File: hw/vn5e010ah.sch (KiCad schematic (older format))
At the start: 5 parts, among them U1001 VN5E010AH

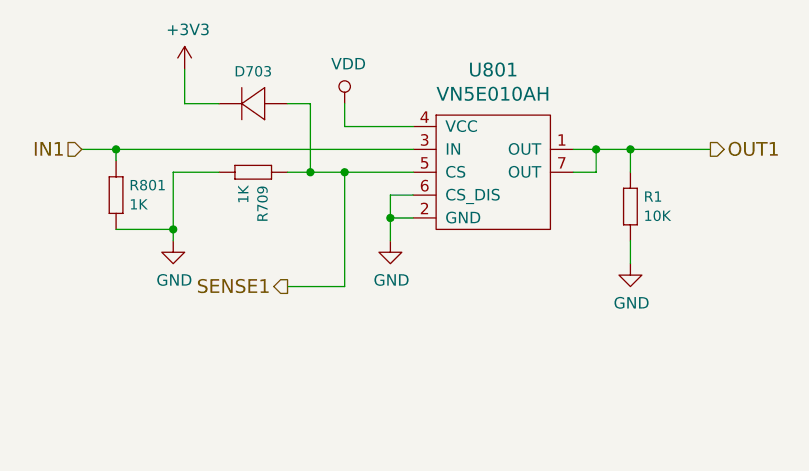
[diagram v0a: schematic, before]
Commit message: sense protection diodes replaced to zeners
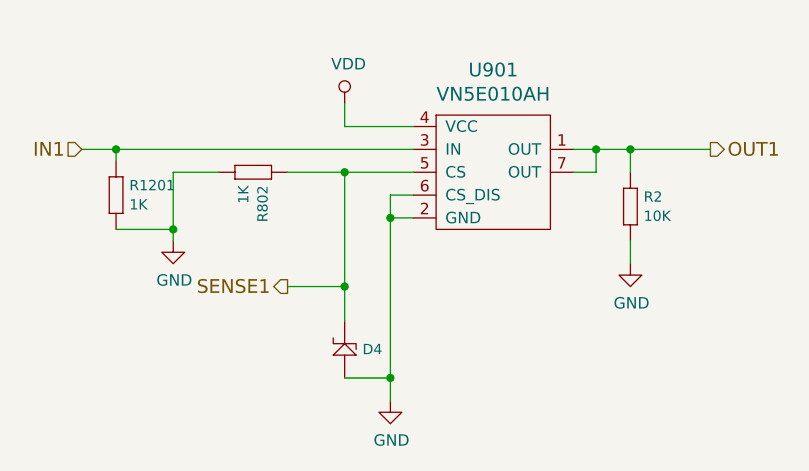
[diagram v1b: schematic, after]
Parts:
- removed D1201: DIODE_RS07J-GS18, usevolt:DO219AB, symbol usevolt:DIODE_RS07J-GS18
- added D3: ZENER_MM3Z3V6T1G, usevolt:SOD-323, symbol usevolt:ZENER_MM3Z3V6T1G
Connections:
- net GND: now also D3.2
- net SENSE1: now also D3.1
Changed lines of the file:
@@
 $Descr A4 11693 8268
 encoding utf-8
-Sheet 7 12
+Sheet 8 12
 Title ""
 Date ""
@@
 SENSE1
 Wire Wire Line
-	4350 3300 4450 3300
-Wire Wire Line
 	3850 3300 4050 3300
 Wire Wire Line
@@
 AR Path="/5A13680F/59D7E637" Ref="#PWR048"  Part="1"
 AR Path="/5A14370A/59D7E637" Ref="#PWR051"  Part="1"
-F 0 "#PWR036" H 4600 2850 50  0001 C CNN
+F 0 "#PWR039" H 4600 2850 50  0001 C CNN
 F 1 "VDD" H 4617 3173 50  0000 C CNN
 F 2 "" H 4600 3000 50  0000 C CNN
@@
 AR Path="/5A13680F/5A014ACD" Ref="#PWR049"  Part="1"
 AR Path="/5A14370A/5A014ACD" Ref="#PWR052"  Part="1"
-F 0 "#PWR037" H 3850 3350 50  0001 C CNN
+F 0 "#PWR040" H 3850 3350 50  0001 C CNN
 F 1 "GND" H 3855 3427 50  0000 C CNN
 F 2 "" H 3850 3600 50  0000 C CNN
@@
 AR Path="/5A13680F/5A058D94" Ref="R1502"  Part="1"
 AR Path="/5A14370A/5A058D94" Ref="R1602"  Part="1"
-F 0 "R801" V 3608 3408 45  0000 L CNN
+F 0 "R1201" V 3608 3408 45  0000 L CNN
 F 1 "1K" V 3692 3408 45  0000 L CNN
 F 2 "yageo:0603" H 3630 3500 20  0001 C CNN
@@
 AR Path="/5A1358B0/5A32CF4A" Ref="U1101"  Part="1"
 AR Path="/5A13680F/5A32CF4A" Ref="U1201"  Part="1"
-F 0 "U801" H 5250 3747 60  0000 C CNN
+F 0 "U901" H 5250 3747 60  0000 C CNN
 F 1 "VN5E010AH" H 5250 3641 60  0000 C CNN
 F 2 "usevolt:HPAK" H 4950 4250 60  0001 C CNN
@@
 L power:GND #PWR044
 U 1 1 5A32CF90
-P 4800 3600
+P 4800 4300
 AR Path="/5A1349CF/5A32CF90" Ref="#PWR044"  Part="1"
 AR Path="/5A14370A/5A32CF90" Ref="#PWR053"  Part="1"
@@
 AR Path="/5A1358B0/5A32CF90" Ref="#PWR047"  Part="1"
 AR Path="/5A13680F/5A32CF90" Ref="#PWR050"  Part="1"
-F 0 "#PWR038" H 4800 3350 50  0001 C CNN
-F 1 "GND" H 4805 3427 50  0000 C CNN
-F 2 "" H 4800 3600 50  0000 C CNN
-F 3 "" H 4800 3600 50  0000 C CNN
-	1    4800 3600
+F 0 "#PWR041" H 4800 4050 50  0001 C CNN
+F 1 "GND" H 4805 4127 50  0000 C CNN
+F 2 "" H 4800 4300 50  0000 C CNN
+F 3 "" H 4800 4300 50  0000 C CNN
+	1    4800 4300
 	1    0    0    -1
 $EndComp
@@
 	3850 3550 3850 3600
 Wire Wire Line
-	4800 3500 4800 3600
+	4800 3500 4800 4200
 $Comp
 L yageo:1K R?
@@
 AR Path="/5A13680F/5B23824A" Ref="R1101"  Part="1"
 AR Path="/5A14370A/5B23824A" Ref="R1202"  Part="1"
-F 0 "R709" V 4258 3358 45  0000 L CNN
+F 0 "R802" V 4258 3358 45  0000 L CNN
 F 1 "1K" V 4342 3358 45  0000 L CNN
 F 2 "yageo:0603" H 4280 3450 20  0001 C CNN
@@
 $EndComp
 $Comp
-L usevolt:DIODE_RS07J-GS18 D1201
-U 1 1 5B23844A
-P 4150 3000
-AR Path="/5A14370A/5B23844A" Ref="D1201"  Part="1"
-AR Path="/5A12FF64/5B23844A" Ref="D703"  Part="1"
-AR Path="/5A130D3E/5B23844A" Ref="D801"  Part="1"
-AR Path="/5A1349CF/5B23844A" Ref="D901"  Part="1"
-AR Path="/5A1358B0/5B23844A" Ref="D1001"  Part="1"
-AR Path="/5A13680F/5B23844A" Ref="D1101"  Part="1"
-F 0 "D703" H 4100 2860 45  0000 C CNN
-F 1 "DIODE_RS07J-GS18" H 4170 2940 45  0001 L BNN
-F 2 "usevolt:DO219AB" H 4180 3150 20  0001 C CNN
-F 3 "http://www.vishay.com/docs/85742/rs07b.pdf" H 4170 3020 60  0001 C CNN
-F 4 "1864882" H 4770 3620 60  0001 C CNN "2nd Source Part Number"
-F 5 "Digi-Key" H 4470 3320 60  0001 C CNN "1st Source"
-F 6 "Farnell" H 4670 3520 60  0001 C CNN "2nd Source"
-F 7 "RS07J-GS18" H 4370 3220 60  0001 C CNN "Manufacturer Part Number"
-F 8 "RS07J-GS18-ND" H 4570 3420 60  0001 C CNN "1st Source Part Number"
-F 9 "Vishay Semiconductor Diodes Division" H 4270 3120 60  0001 C CNN "Manufacturer"
-	1    4150 3000
-	-1   0    0    1
-$EndComp
-$Comp
-L power:+3V3 #PWR0107
-U 1 1 5B23856B
-P 3900 2850
-AR Path="/5A14370A/5B23856B" Ref="#PWR0107"  Part="1"
-AR Path="/5A12FF64/5B23856B" Ref="#PWR0102"  Part="1"
-AR Path="/5A130D3E/5B23856B" Ref="#PWR0103"  Part="1"
-AR Path="/5A1349CF/5B23856B" Ref="#PWR0104"  Part="1"
-AR Path="/5A1358B0/5B23856B" Ref="#PWR0105"  Part="1"
-AR Path="/5A13680F/5B23856B" Ref="#PWR0106"  Part="1"
-F 0 "#PWR0102" H 3900 2700 50  0001 C CNN
-F 1 "+3V3" H 3915 3023 50  0000 C CNN
-F 2 "" H 3900 2850 50  0000 C CNN
-F 3 "" H 3900 2850 50  0000 C CNN
-	1    3900 2850
-	1    0    0    -1
-$EndComp
-Wire Wire Line
-	3900 2850 3900 3000
-Wire Wire Line
-	3900 3000 4050 3000
-Wire Wire Line
-	4350 3000 4450 3000
-Wire Wire Line
-	4450 3000 4450 3300
-Connection ~ 4450 3300
-Wire Wire Line
-	4450 3300 4600 3300
-$Comp
 L yageo:10K R1
 U 1 1 5BA9BFAA
@@
 AR Path="/5A1349CF/5BA9BFAA" Ref="R3"  Part="1"
 AR Path="/5A1358B0/5BA9BFAA" Ref="R4"  Part="1"
-F 0 "R1" V 5858 3458 45  0000 L CNN
+F 0 "R2" V 5858 3458 45  0000 L CNN
 F 1 "10K" V 5942 3458 45  0000 L CNN
 F 2 "yageo:0603" H 5880 3550 20  0001 C CNN
@@
 AR Path="/5A1349CF/5BA9C33E" Ref="#PWR0108"  Part="1"
 AR Path="/5A1358B0/5BA9C33E" Ref="#PWR0109"  Part="1"
-F 0 "#PWR0106" H 5850 3450 50  0001 C CNN
+F 0 "#PWR0107" H 5850 3450 50  0001 C CNN
 F 1 "GND" H 5855 3527 50  0000 C CNN
 F 2 "" H 5850 3700 50  0000 C CNN
@@
 Wire Wire Line
 	5850 3700 5850 3600
+Wire Wire Line
+	4350 3300 4600 3300
+$Comp
+L usevolt:ZENER_MM3Z3V6T1G D3
+U 1 1 5BAABE3C
+P 4600 4000
+AR Path="/5A12FF64/5BAABE3C" Ref="D3"  Part="1"
+AR Path="/5A130D3E/5BAABE3C" Ref="D4"  Part="1"
+AR Path="/5A1349CF/5BAABE3C" Ref="D5"  Part="1"
+AR Path="/5A1358B0/5BAABE3C" Ref="D6"  Part="1"
+F 0 "D4" V 4525 3922 45  0000 R CNN
+F 1 "ZENER_MM3Z3V6T1G" H 4875 4375 45  0001 L BNN
+F 2 "usevolt:SOD-323" H 4575 4375 20  0001 C CNN
+F 3 "http://www.mouser.com/ds/2/308/MM3Z2V4T1-D-269162.pdf" H 4950 4575 60  0001 C CNN
+F 4 "Mouser" H 4920 4320 60  0001 C CNN "1st Source"
+F 5 "MM3Z3V6T1G" H 4820 4220 60  0001 C CNN "Manufacturer Part Number"
+F 6 "863-MM3Z3V6T1G" H 5020 4420 60  0001 C CNN "1st Source Part Number"
+F 7 "ON Semiconductor" H 4875 4475 60  0001 C CNN "Manufacturer"
+	1    4600 4000
+	0    -1   -1   0
+$EndComp
+Wire Wire Line
+	4600 3950 4600 3800
+Connection ~ 4600 3800
+Wire Wire Line
+	4600 4200 4800 4200
+Connection ~ 4800 4200
+Wire Wire Line
+	4800 4200 4800 4300
 $EndSCHEMATC

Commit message: radiator fet added to pcb, but not yet ready
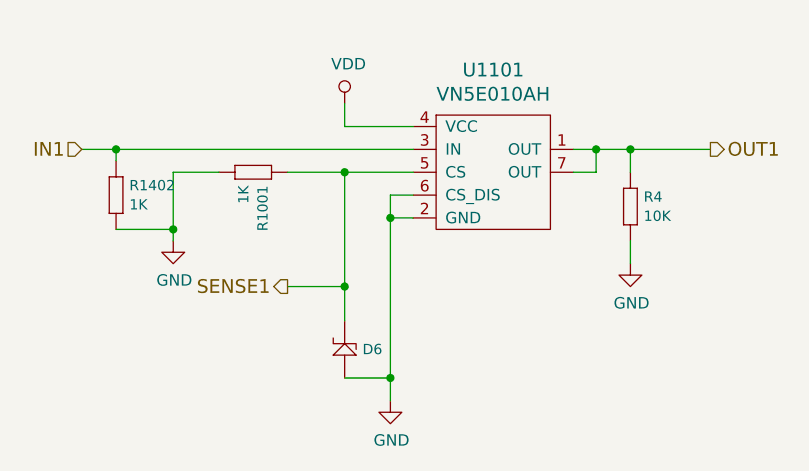
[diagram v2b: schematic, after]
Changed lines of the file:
@@
 $Descr A4 11693 8268
 encoding utf-8
-Sheet 8 12
+Sheet 8 13
 Title ""
 Date ""
@@
 AR Path="/5A13680F/59D7E637" Ref="#PWR048"  Part="1"
 AR Path="/5A14370A/59D7E637" Ref="#PWR051"  Part="1"
-F 0 "#PWR039" H 4600 2850 50  0001 C CNN
+F 0 "#PWR045" H 4600 2850 50  0001 C CNN
 F 1 "VDD" H 4617 3173 50  0000 C CNN
 F 2 "" H 4600 3000 50  0000 C CNN
@@
 AR Path="/5A13680F/5A014ACD" Ref="#PWR049"  Part="1"
 AR Path="/5A14370A/5A014ACD" Ref="#PWR052"  Part="1"
-F 0 "#PWR040" H 3850 3350 50  0001 C CNN
+F 0 "#PWR046" H 3850 3350 50  0001 C CNN
 F 1 "GND" H 3855 3427 50  0000 C CNN
 F 2 "" H 3850 3600 50  0000 C CNN
@@
 AR Path="/5A13680F/5A058D94" Ref="R1502"  Part="1"
 AR Path="/5A14370A/5A058D94" Ref="R1602"  Part="1"
-F 0 "R1201" V 3608 3408 45  0000 L CNN
+F 0 "R1402" V 3608 3408 45  0000 L CNN
 F 1 "1K" V 3692 3408 45  0000 L CNN
 F 2 "yageo:0603" H 3630 3500 20  0001 C CNN
@@
 AR Path="/5A1358B0/5A32CF4A" Ref="U1101"  Part="1"
 AR Path="/5A13680F/5A32CF4A" Ref="U1201"  Part="1"
-F 0 "U901" H 5250 3747 60  0000 C CNN
+F 0 "U1101" H 5250 3747 60  0000 C CNN
 F 1 "VN5E010AH" H 5250 3641 60  0000 C CNN
 F 2 "usevolt:HPAK" H 4950 4250 60  0001 C CNN
@@
 AR Path="/5A1358B0/5A32CF90" Ref="#PWR047"  Part="1"
 AR Path="/5A13680F/5A32CF90" Ref="#PWR050"  Part="1"
-F 0 "#PWR041" H 4800 4050 50  0001 C CNN
+F 0 "#PWR047" H 4800 4050 50  0001 C CNN
 F 1 "GND" H 4805 4127 50  0000 C CNN
 F 2 "" H 4800 4300 50  0000 C CNN
@@
 AR Path="/5A13680F/5B23824A" Ref="R1101"  Part="1"
 AR Path="/5A14370A/5B23824A" Ref="R1202"  Part="1"
-F 0 "R802" V 4258 3358 45  0000 L CNN
+F 0 "R1001" V 4258 3358 45  0000 L CNN
 F 1 "1K" V 4342 3358 45  0000 L CNN
 F 2 "yageo:0603" H 4280 3450 20  0001 C CNN
@@
 AR Path="/5A1349CF/5BA9BFAA" Ref="R3"  Part="1"
 AR Path="/5A1358B0/5BA9BFAA" Ref="R4"  Part="1"
-F 0 "R2" V 5858 3458 45  0000 L CNN
+F 0 "R4" V 5858 3458 45  0000 L CNN
 F 1 "10K" V 5942 3458 45  0000 L CNN
 F 2 "yageo:0603" H 5880 3550 20  0001 C CNN
@@
 AR Path="/5A1349CF/5BA9C33E" Ref="#PWR0108"  Part="1"
 AR Path="/5A1358B0/5BA9C33E" Ref="#PWR0109"  Part="1"
-F 0 "#PWR0107" H 5850 3450 50  0001 C CNN
+F 0 "#PWR0109" H 5850 3450 50  0001 C CNN
 F 1 "GND" H 5855 3527 50  0000 C CNN
 F 2 "" H 5850 3700 50  0000 C CNN
@@
 AR Path="/5A1349CF/5BAABE3C" Ref="D5"  Part="1"
 AR Path="/5A1358B0/5BAABE3C" Ref="D6"  Part="1"
-F 0 "D4" V 4525 3922 45  0000 R CNN
+F 0 "D6" V 4525 3922 45  0000 R CNN
 F 1 "ZENER_MM3Z3V6T1G" H 4875 4375 45  0001 L BNN
 F 2 "usevolt:SOD-323" H 4575 4375 20  0001 C CNN

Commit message: reorganazing pcb with 4 fets on radiator
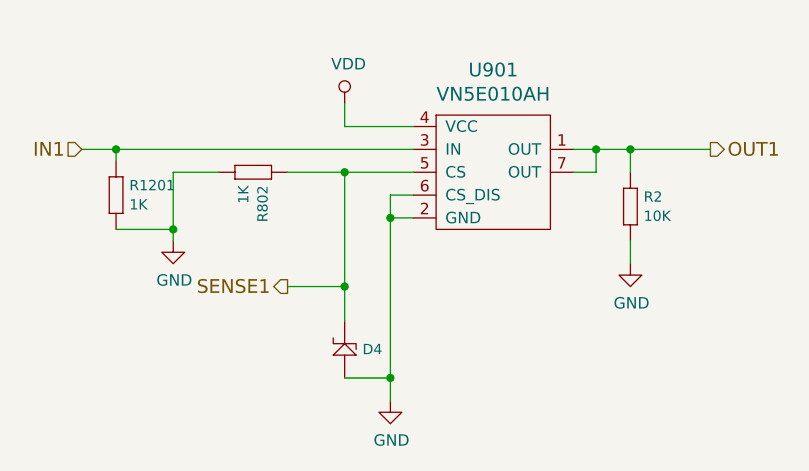
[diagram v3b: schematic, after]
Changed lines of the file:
@@
 AR Path="/5A13680F/59D7E637" Ref="#PWR048"  Part="1"
 AR Path="/5A14370A/59D7E637" Ref="#PWR051"  Part="1"
-F 0 "#PWR045" H 4600 2850 50  0001 C CNN
+F 0 "#PWR039" H 4600 2850 50  0001 C CNN
 F 1 "VDD" H 4617 3173 50  0000 C CNN
 F 2 "" H 4600 3000 50  0000 C CNN
@@
 AR Path="/5A13680F/5A014ACD" Ref="#PWR049"  Part="1"
 AR Path="/5A14370A/5A014ACD" Ref="#PWR052"  Part="1"
-F 0 "#PWR046" H 3850 3350 50  0001 C CNN
+F 0 "#PWR040" H 3850 3350 50  0001 C CNN
 F 1 "GND" H 3855 3427 50  0000 C CNN
 F 2 "" H 3850 3600 50  0000 C CNN
@@
 AR Path="/5A13680F/5A058D94" Ref="R1502"  Part="1"
 AR Path="/5A14370A/5A058D94" Ref="R1602"  Part="1"
-F 0 "R1402" V 3608 3408 45  0000 L CNN
+F 0 "R1201" V 3608 3408 45  0000 L CNN
 F 1 "1K" V 3692 3408 45  0000 L CNN
 F 2 "yageo:0603" H 3630 3500 20  0001 C CNN
@@
 AR Path="/5A1358B0/5A32CF4A" Ref="U1101"  Part="1"
 AR Path="/5A13680F/5A32CF4A" Ref="U1201"  Part="1"
-F 0 "U1101" H 5250 3747 60  0000 C CNN
+F 0 "U901" H 5250 3747 60  0000 C CNN
 F 1 "VN5E010AH" H 5250 3641 60  0000 C CNN
 F 2 "usevolt:HPAK" H 4950 4250 60  0001 C CNN
@@
 AR Path="/5A1358B0/5A32CF90" Ref="#PWR047"  Part="1"
 AR Path="/5A13680F/5A32CF90" Ref="#PWR050"  Part="1"
-F 0 "#PWR047" H 4800 4050 50  0001 C CNN
+F 0 "#PWR041" H 4800 4050 50  0001 C CNN
 F 1 "GND" H 4805 4127 50  0000 C CNN
 F 2 "" H 4800 4300 50  0000 C CNN
@@
 AR Path="/5A13680F/5B23824A" Ref="R1101"  Part="1"
 AR Path="/5A14370A/5B23824A" Ref="R1202"  Part="1"
-F 0 "R1001" V 4258 3358 45  0000 L CNN
+F 0 "R802" V 4258 3358 45  0000 L CNN
 F 1 "1K" V 4342 3358 45  0000 L CNN
 F 2 "yageo:0603" H 4280 3450 20  0001 C CNN
@@
 AR Path="/5A1349CF/5BA9BFAA" Ref="R3"  Part="1"
 AR Path="/5A1358B0/5BA9BFAA" Ref="R4"  Part="1"
-F 0 "R4" V 5858 3458 45  0000 L CNN
+F 0 "R2" V 5858 3458 45  0000 L CNN
 F 1 "10K" V 5942 3458 45  0000 L CNN
 F 2 "yageo:0603" H 5880 3550 20  0001 C CNN
@@
 AR Path="/5A1349CF/5BA9C33E" Ref="#PWR0108"  Part="1"
 AR Path="/5A1358B0/5BA9C33E" Ref="#PWR0109"  Part="1"
-F 0 "#PWR0109" H 5850 3450 50  0001 C CNN
+F 0 "#PWR0107" H 5850 3450 50  0001 C CNN
 F 1 "GND" H 5855 3527 50  0000 C CNN
 F 2 "" H 5850 3700 50  0000 C CNN
@@
 AR Path="/5A1349CF/5BAABE3C" Ref="D5"  Part="1"
 AR Path="/5A1358B0/5BAABE3C" Ref="D6"  Part="1"
-F 0 "D6" V 4525 3922 45  0000 R CNN
+F 0 "D4" V 4525 3922 45  0000 R CNN
 F 1 "ZENER_MM3Z3V6T1G" H 4875 4375 45  0001 L BNN
 F 2 "usevolt:SOD-323" H 4575 4375 20  0001 C CNN
